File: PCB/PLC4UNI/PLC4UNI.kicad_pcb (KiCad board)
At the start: 4 copper layers, 102.4 x 83.1 mm, 209 parts, among them J1 Conn_02x08_Odd_Even, K1 G5V-1-DC3, K2 G5V-1-DC3, Q1 ZXMS6004FFQTA, Q2 ZXMS6004FFQTA, Q3 ZXMS6004FFQTA, Q4 ZXMS6004FFQTA, Q5 NCE60P04R, SW1 TS-1088-AR02016, SW2 TS-1088-AR02016, U1 ScrewTerminal1-1x9-P5.0mm, U10 AT3H4B-CUH-S, U11 AT3H4B-CUH-S, U12 AT3H4B-CUH-S, U13 AT3H4B-CUH-S, U14 AT3H4B-CUH-S, U15 MAX31856MUD+, U16 GP8211S-TC50-EW, U17 GP8302-TC50-EW, U18 BL0942, U19 B0303S-1WR3_C7465185, U2 ScrewTerminal1-1x9-P5.0mm, U20 ISO7021DR, U21 AP63203WU-7, U22 APH0630T4R7M, U23 TD301M485_C5451847, U3 ScrewTerminal1-1x9-P5.0mm, U4 ScrewTerminal1-1x9-P5.0mm, U5 ADS1115IDGS, U6 ESP32-S3-WROOM-1, U7 BTS723GWXUMA1, U8 LK1802, U9 AT3H4B-CUH-S

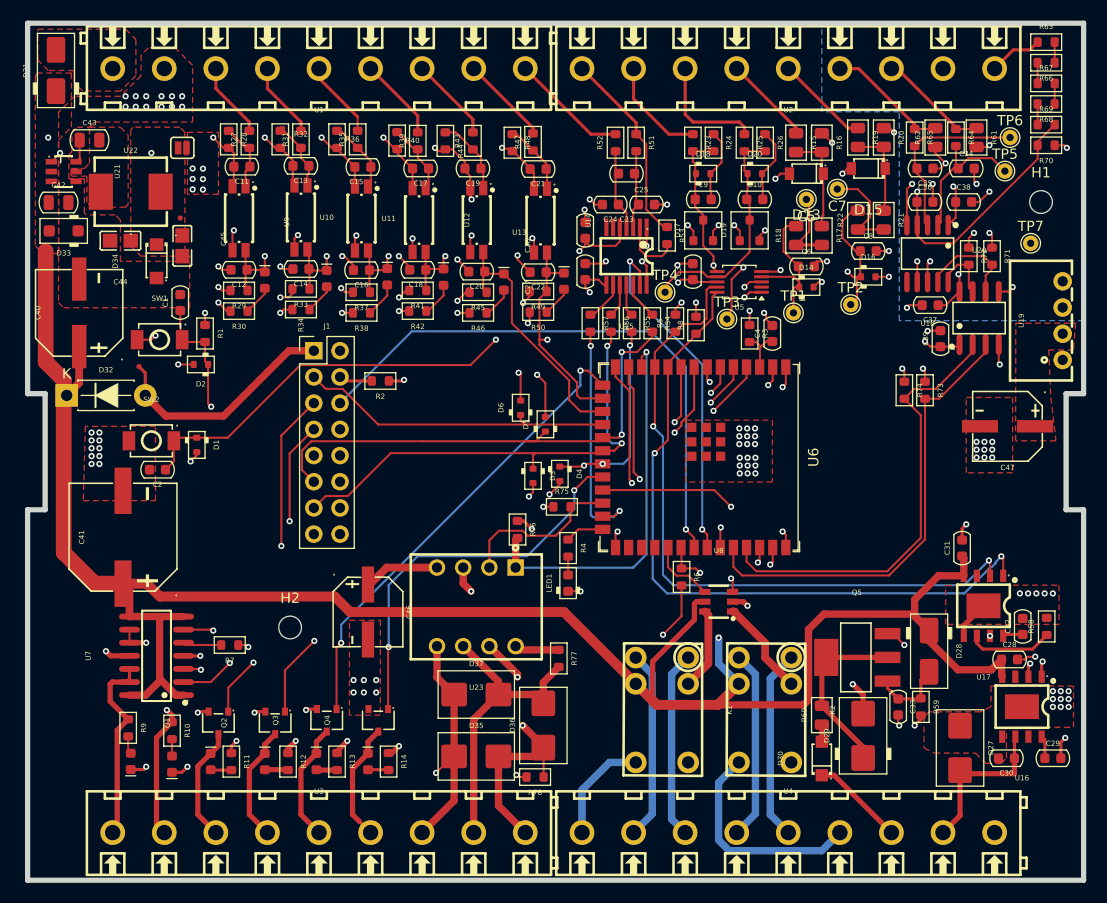
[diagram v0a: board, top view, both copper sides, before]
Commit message: re-enrrutado
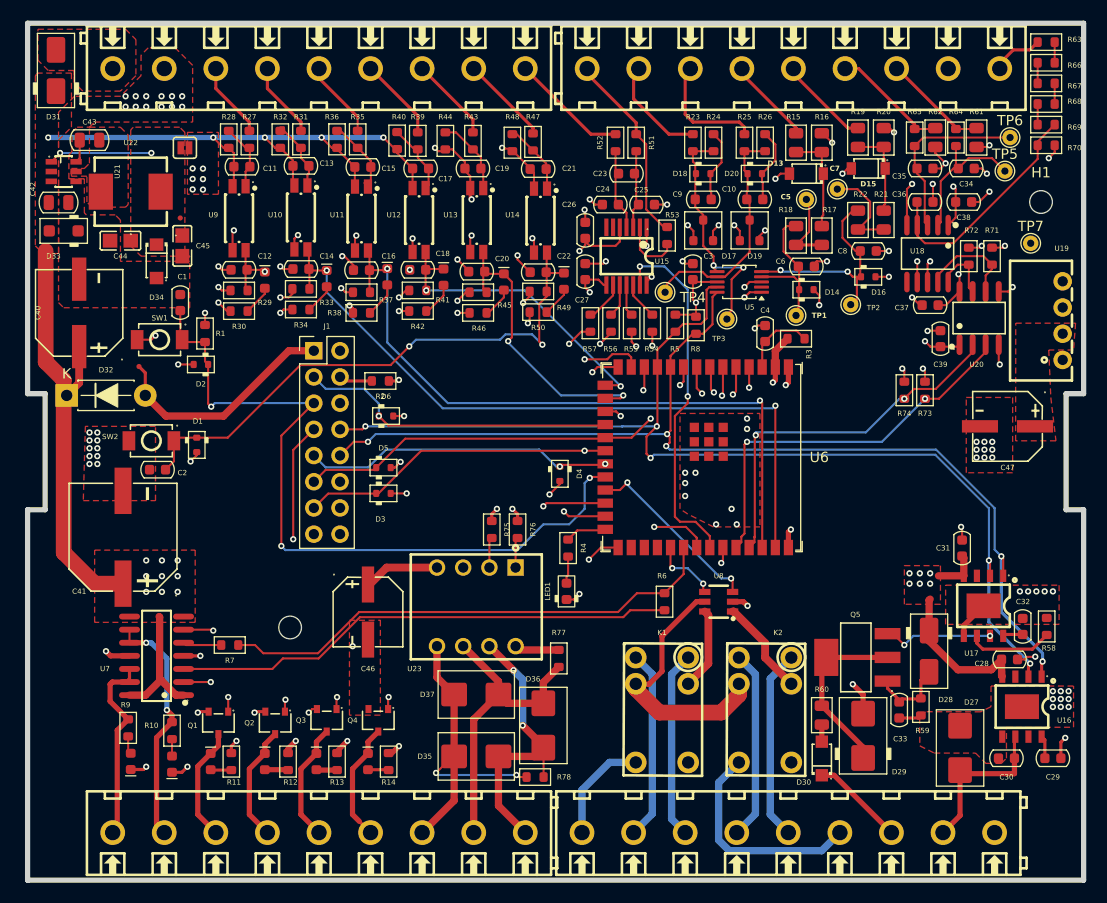
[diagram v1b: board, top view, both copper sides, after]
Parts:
- moved D5 16.3 mm to (188.4, 127.7), turned to 0 degrees
- moved D3 14.6 mm to (188.4, 130.2), turned to 0 degrees
- moved D6 13.1 mm to (188.7, 122.7), turned to 0 degrees
- moved R75 7.15 mm to (198.9, 133.7), turned to -90 degrees
- moved R3 4.53 mm to (228.4, 115.2), turned to 0 degrees
- moved R6 2.91 mm to (215.7, 140.7)
- moved LED1 0.81 mm to (206.2, 139.7)
- moved C4 0.70 mm to (225.4, 114.7)
- moved U2 0.50 mm to (228.2, 89.0)
- moved TP1 0.35 mm to (228.4, 112.9)
- moved C33 0.32 mm to (238.4, 151.2)
- moved D14 0.25 mm to (229.4, 110.4)
- moved JP1 0.25 mm to (169.2, 96.7)
- moved U6 0.25 mm to (219.4, 126.7)
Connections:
- U6 pad 15: /plc4uni_top/OUT_NPN3 -> /plc4uni_top/IN_NPN4
- U6 pad 16: /plc4uni_top/IN_PNP2 -> /plc4uni_top/IN_PNP1
- U6 pad 17: /plc4uni_top/IN_PNP1 -> /plc4uni_top/RS485-TX
- U6 pad 22: /plc4uni_top/OUT_NPN4 -> /plc4uni_top/RESET
- U6 pad 24: /plc4uni_top/RS485-TX -> /plc4uni_top/IN_PNP2
- U6 pad 27: /plc4uni_top/RESET -> /plc4uni_top/IN_NPN1
- U6 pad 38: /plc4uni_top/OUT_NPN2 -> /plc4uni_top/IN_NPN3
- U6 pad 39: /plc4uni_top/OUT_NPN1 -> /plc4uni_top/IN_NPN2
- U6 pad 4: /plc4uni_top/IN_NPN1 -> /plc4uni_top/OUT_NPN1
- U6 pad 5: /plc4uni_top/IN_NPN2 -> /plc4uni_top/OUT_NPN2
- U6 pad 6: /plc4uni_top/IN_NPN3 -> /plc4uni_top/OUT_NPN3
- U6 pad 7: /plc4uni_top/IN_NPN4 -> /plc4uni_top/OUT_NPN4
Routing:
- net VCC: track 255.8 -> 233.8 mm, vias 6 -> 20
- net /plc4uni_top/OUT_NPN4: track 38.2 -> 55.4 mm
- net /plc4uni_top/OUT_NPN3: track 45.3 -> 62.2 mm
- net /plc4uni_top/IN_NPN4: track 45.6 -> 29.8 mm
- net /plc4uni_top/IN_NPN3: track 50.5 -> 66.1 mm
- net /plc4uni_top/OUT_NPN1: track 61.6 -> 75.7 mm
- net /plc4uni_top/OUT_NPN2: track 55.7 -> 68.3 mm
- net /plc4uni_top/IN_PNP2: track 64.7 -> 77.0 mm, vias 2 -> 3
- net /plc4uni_top/TP_INT: track 55.7 -> 44.3 mm
- net /plc4uni_top/IN_NPN2: track 58.6 -> 69.8 mm
- net GND: track 114.2 -> 103.1 mm, vias 130 -> 113
- net /plc4uni_top/RS485-TX: track 16.3 -> 27.3 mm, vias 0 -> 1
- net /plc4uni_top/USB+: track 41.2 -> 32.6 mm
- net /plc4uni_top/RS485-RX: track 37.4 -> 30.0 mm
- net /plc4uni_top/I2C_SCK: track 112.3 -> 104.9 mm, vias 3 -> 5
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- added copper zone on In2.Cu, net Earth
- added copper zone on In2.Cu, net GND
- added copper zone on In2.Cu, net VCC
- removed copper zone on B.Cu, net Earth
- removed copper zone on B.Cu, net GND

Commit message: ensamblado en proceso
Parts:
- moved U4 0.83 mm to (228.4, 163.4)
- moved U2 0.50 mm to (228.7, 89.0)
- moved U3 0.37 mm to (182.2, 163.4)
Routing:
- net /plc4uni_top/CON_OUT_RLY2-COM: track 21.3 -> 22.7 mm
- net /plc4uni_top/CON_OUT_RLY1-NO: track 18.2 -> 19.1 mm
- net /plc4uni_top/CON_OUT_4-20MA_1: track 9.05 -> 9.95 mm
- net /plc4uni_top/CON_OUT_RLY2-NO: track 18.5 -> 19.4 mm
- net /plc4uni_top/CON_OUT_RLY1-COM: track 10.5 -> 11.1 mm
- net /plc4uni_top/CON_IN_0-10V_1: track 10.3 -> 10.8 mm
- net /plc4uni_top/CON_IN_0-10V_2: track 11.6 -> 12.1 mm

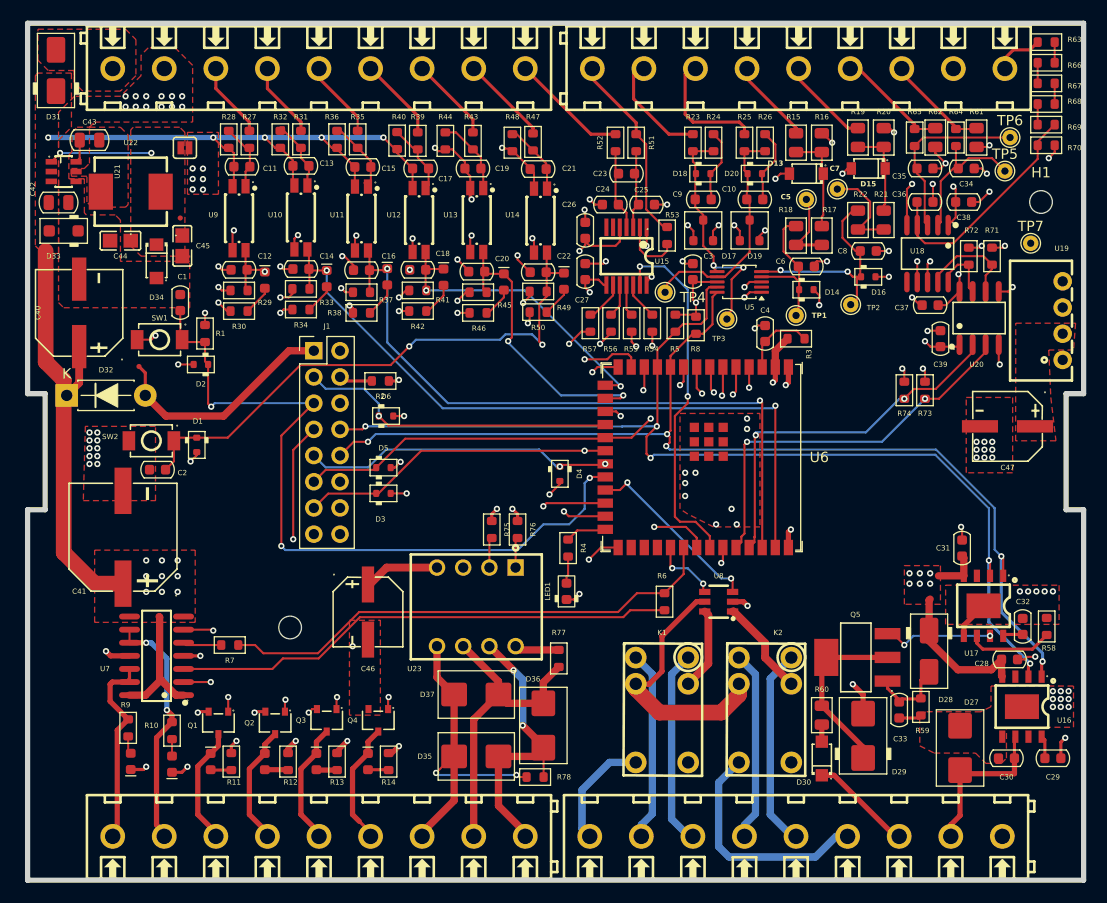
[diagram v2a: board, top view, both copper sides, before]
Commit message: PCBUNI y MEZANINI añadida
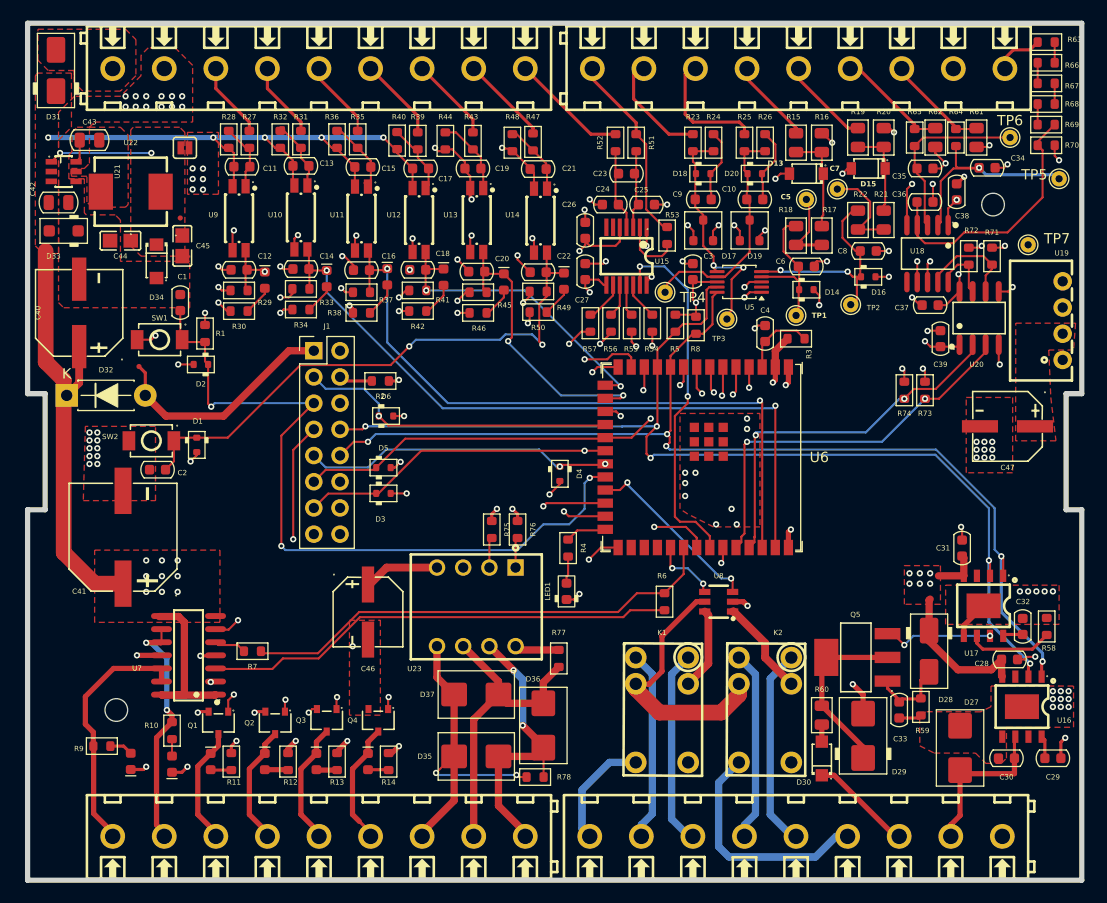
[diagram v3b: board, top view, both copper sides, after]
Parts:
- moved H2 18.7 mm to (162.5, 151.2)
- moved TP5 5.30 mm to (253.9, 99.7)
- moved H1 4.66 mm to (247.5, 102.2)
- moved R9 3.10 mm to (161.1, 154.7), turned to 0 degrees
- moved U7 3.10 mm to (169.5, 145.9)
- moved R7 2.28 mm to (175.7, 145.5)
- moved C34 2.02 mm to (246.9, 98.6)
- moved C38 1.20 mm to (244.0, 100.9), turned to 90 degrees
- moved TP7 0.29 mm to (250.9, 106.1)
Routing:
- net Net-(U18-IP): track 14.3 -> 21.1 mm, vias 0 -> 1
- net /plc4uni_top/CON_OUT_PNP1: track 19.4 -> 24.4 mm
- net VCC: track 234.3 -> 237.4 mm
- net /plc4uni_top/OUT_PNP2: track 65.2 -> 62.0 mm
- net /plc4uni_top/OUT-PNP/ST1: track 49.0 -> 45.9 mm
- net Net-(U18-VP): track 22.6 -> 25.5 mm
- net /plc4uni_top/ST1_ST2: track 49.3 -> 46.8 mm
- net /plc4uni_top/OUT_PNP1: track 70.3 -> 68.2 mm
- net 3.3V_P: track 13.2 -> 11.9 mm
- net Earth: track 20.6 -> 19.5 mm
- net /plc4uni_top/OUT-PNP/ST2: track 3.75 -> 3.12 mm
- net Net-(D7-A): track 1.74 -> 2.26 mm
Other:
- board size 102.4 x 83.1 mm -> 102.2 x 83.1 mm

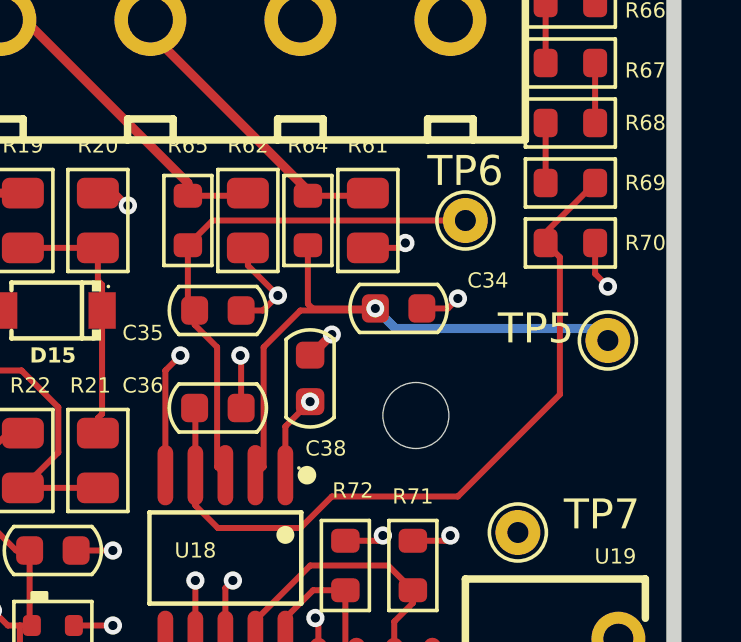
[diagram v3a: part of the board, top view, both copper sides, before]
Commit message: Fixed joint base y pcb plcuni
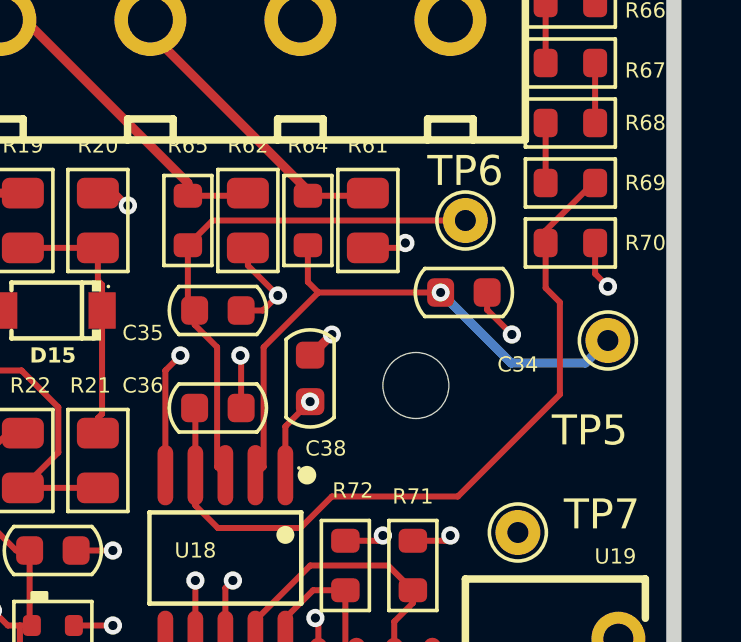
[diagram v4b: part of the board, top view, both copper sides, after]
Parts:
- moved C34 2.24 mm to (249.1, 98.1)
- moved H1 1.00 mm to (247.5, 101.2)
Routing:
- net Net-(U18-IP): track 21.1 -> 19.6 mm
